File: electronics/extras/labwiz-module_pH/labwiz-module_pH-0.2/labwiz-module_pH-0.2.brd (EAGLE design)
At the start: 15.8 x 31.5 mm, 14 parts, among them U3 XC6206P182MR, U4 OPA333DBV

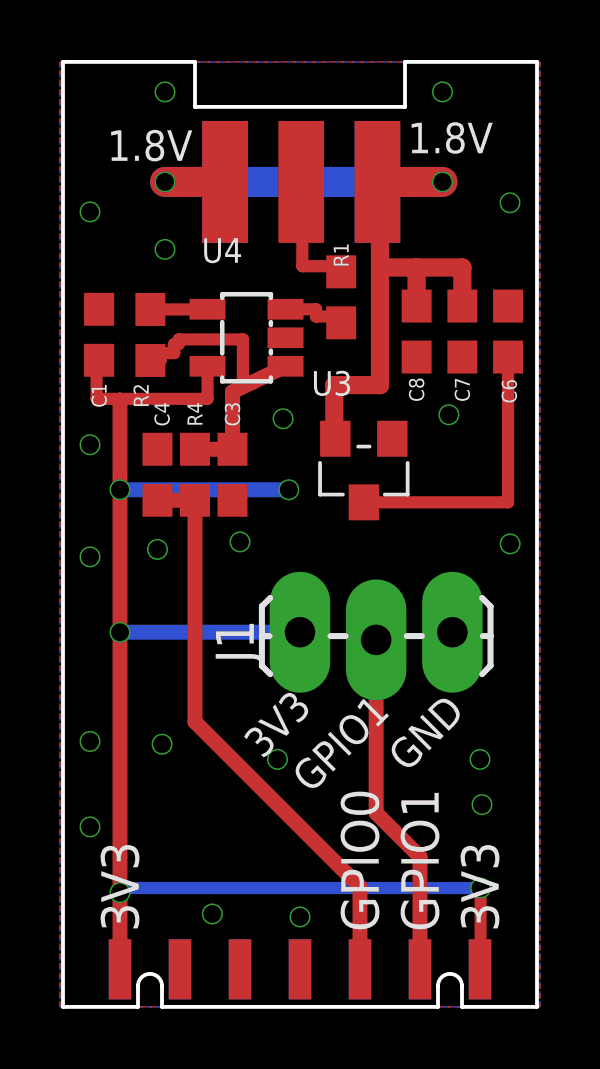
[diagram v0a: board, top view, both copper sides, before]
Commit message: Fixed VBUS issues on pH module.
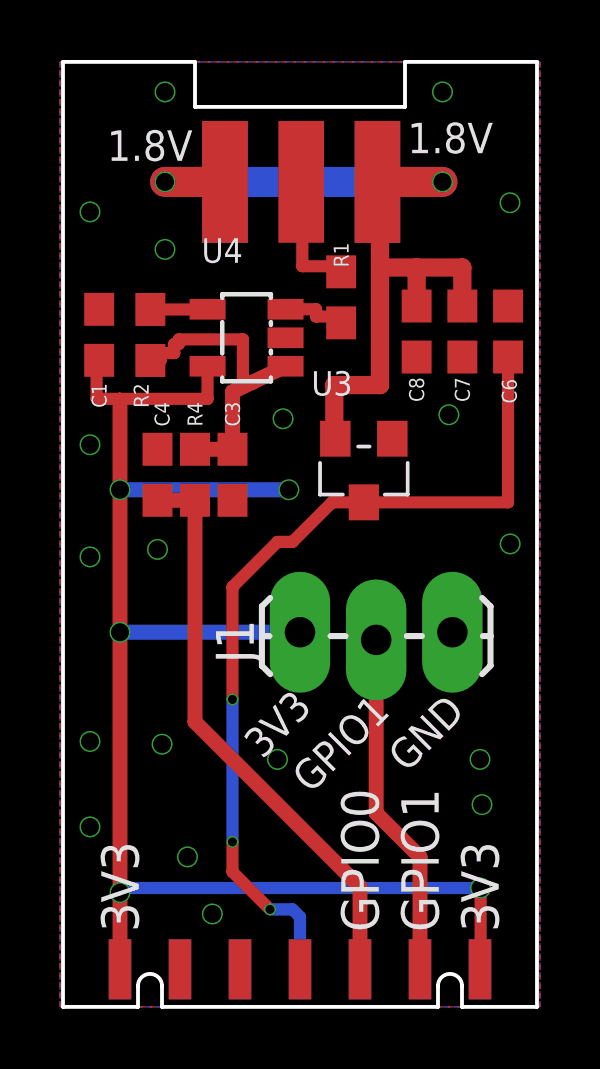
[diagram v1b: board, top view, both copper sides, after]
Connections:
- net VBUS: now also MODULE5.P$8
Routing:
- net VBUS: track 9.65 -> 29.3 mm, vias 0 -> 3
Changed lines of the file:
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@@
 <via x="1" y="18.738" extent="1-16" drill="0.6" shape="square"/>
 <via x="14" y="8.25" extent="1-16" drill="0.6" shape="square"/>
-<via x="6" y="15.5" extent="1-16" drill="0.6" shape="square"/>
 <via x="15.0052" y="15.4332" extent="1-16" drill="0.6" shape="square"/>
 <via x="7.25" y="8.25" extent="1-16" drill="0.6" shape="square"/>
 <via x="14.0668" y="6.7432" extent="1-16" drill="0.6" shape="square"/>
-<via x="8" y="3" extent="1-16" drill="0.6" shape="square"/>
+<via x="4.25" y="5" extent="1-16" drill="0.6" shape="square"/>
 <via x="1" y="26.5" extent="1-16" drill="0.6" shape="square"/>
 <via x="15" y="26.8048" extent="1-16" drill="0.6" shape="square"/>
@@
 <wire x1="10.1284" y1="16.8184" x2="14.9352" y2="16.8184" width="0.4064" layer="1"/>
 <wire x1="14.9352" y1="16.8184" x2="14.9352" y2="21.6624" width="0.4064" layer="1"/>
+<contactref element="MODULE5" pad="P$8"/>
+<wire x1="10.1284" y1="16.8184" x2="9.0684" y2="16.8184" width="0.4064" layer="1"/>
+<wire x1="9.0684" y1="16.8184" x2="7.75" y2="15.5" width="0.4064" layer="1"/>
+<wire x1="7.75" y1="15.5" x2="7.25" y2="15.5" width="0.4064" layer="1"/>
+<wire x1="7.25" y1="15.5" x2="5.75" y2="14" width="0.4064" layer="1"/>
+<wire x1="5.75" y1="14" x2="5.75" y2="10.25" width="0.4064" layer="1"/>
+<via x="5.75" y="10.25" extent="1-16" drill="0.3" shape="square"/>
+<wire x1="5.75" y1="10.25" x2="5.75" y2="5.5" width="0.4064" layer="16"/>
+<via x="5.75" y="5.5" extent="1-16" drill="0.3" shape="square"/>
+<wire x1="5.75" y1="5.5" x2="5.75" y2="4.5" width="0.4064" layer="1"/>
+<wire x1="5.75" y1="4.5" x2="7" y2="3.25" width="0.4064" layer="1"/>
+<via x="7" y="3.25" extent="1-16" drill="0.3" shape="square"/>
+<wire x1="7" y1="3.25" x2="7.75" y2="3.25" width="0.4064" layer="16"/>
+<wire x1="7.75" y1="3.25" x2="8" y2="3" width="0.4064" layer="16"/>
+<wire x1="8" y1="3" x2="8" y2="1.25" width="0.4064" layer="16"/>
 </signal>
 </signals>

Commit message: Small changes. Not sure what.
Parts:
- C3, C4: value (none) -> 51pF
- R1, R2: value (none) -> 510k
- R4: value (none) -> 51k
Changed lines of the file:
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@@
 <attribute name="VALUE" x="8.738" y="15.5136" size="0.5" layer="27" font="vector" ratio="10"/>
 </element>
-<element name="R1" library="PaxInstruments-RCL" package="0603" value="" x="9.3716" y="23.6524" smashed="yes" rot="R270">
+<element name="R1" library="PaxInstruments-RCL" package="0603" value="510k" x="9.3716" y="23.6524" smashed="yes" rot="R270">
 <attribute name="NAME" x="9.3716" y="24.6524" size="0.5" layer="25" font="vector" rot="R270" align="center-right"/>
 <attribute name="VALUE" value="" x="9.3716" y="22.6524" size="0.5" layer="27" rot="R270" align="center-left"/>
@@
 <attribute name="VALUE" value="100nF" x="1.3048" y="24.012" size="0.5" layer="27" font="vector" rot="R90" align="center-left"/>
 </element>
-<element name="R2" library="PaxInstruments-RCL" package="0603" value="" x="3.012" y="22.3976" smashed="yes" rot="R90">
+<element name="R2" library="PaxInstruments-RCL" package="0603" value="510k" x="3.012" y="22.3976" smashed="yes" rot="R90">
 <attribute name="NAME" x="2.7072" y="20.788" size="0.5" layer="25" font="vector" rot="R90" align="center-right"/>
 <attribute name="VALUE" value="" x="3.012" y="23.3976" size="0.5" layer="27" rot="R90" align="center-left"/>
 </element>
-<element name="C3" library="PaxInstruments-RCL" package="0603" value="" x="5.75" y="17.738" smashed="yes" rot="R90">
+<element name="C3" library="PaxInstruments-RCL" package="0603" value="51pF" x="5.75" y="17.738" smashed="yes" rot="R90">
 <attribute name="NAME" x="5.75" y="19.3476" size="0.5" layer="25" font="vector" rot="R270" align="center-right"/>
 <attribute name="VALUE" value="" x="5.75" y="16.738" size="0.5" layer="27" rot="R270" align="center-left"/>
 </element>
-<element name="R4" library="PaxInstruments-RCL" package="0603" value="" x="4.5" y="17.738" smashed="yes" rot="R270">
+<element name="R4" library="PaxInstruments-RCL" package="0603" value="51k" x="4.5" y="17.738" smashed="yes" rot="R270">
 <attribute name="NAME" x="4.5" y="19.3476" size="0.5" layer="25" font="vector" rot="R270" align="center-right"/>
 <attribute name="VALUE" value="" x="4.5" y="16.738" size="0.5" layer="27" rot="R270" align="center-left"/>
 </element>
-<element name="C4" library="PaxInstruments-RCL" package="0603" value="" x="3.25" y="17.738" smashed="yes" rot="R270">
+<element name="C4" library="PaxInstruments-RCL" package="0603" value="51pF" x="3.25" y="17.738" smashed="yes" rot="R270">
 <attribute name="NAME" x="3.4024" y="19.3476" size="0.5" layer="25" font="vector" rot="R270" align="center-right"/>
 <attribute name="VALUE" value="" x="3.25" y="16.738" size="0.5" layer="27" rot="R270" align="center-left"/>
